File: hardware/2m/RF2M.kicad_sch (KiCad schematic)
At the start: 0 parts

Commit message: Preserve M5A-R1 VHF electrical candidate and review evidence
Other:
- removed sheet 04 2S boost and regulated MMIC rail continued
- note added: "M5A-R1: 144 MHz TRUE AM / EVALUATION SCHEMATIC / NOT RELEASED 1 W ERP sizing: 1.259 W connector carrier, 4.079 W PEP at m=0.80. 2S BOOST or 4S BUCK exclusive populations; training needs only controller 3.3 V. BLOCKING: ST VHF matching not traced; PD54008 PowerFLAT numeric pads OPEN. NO LAYOUT. OPEN: hot SOA, analog loop, RF AM and physical driver-fault response. No PCB/layout/Gerbers/procurement.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"
- note removed: "M5A-R0: 144 MHz TRUE AM / EVALUATION SCHEMATIC / NOT RELEASED\n1 W ERP sizing: 1.259 W connector carrier, 4.079 W PEP at m=0.80.\n2S BOOST or 4S BUCK exclusive populations; training needs only controller 3.3 V.\nOPEN: large-signal matching, hot SOA, critical package geometry, analog loop stability.\nNo PCB/layout/Gerbers/procurement. All physical results NOT_RUN. See docs/M5_2M_REVIEW_DECISION.md."

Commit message: Preserve M5A-R3 historical transmitter schematic and review
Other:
- removed sheet 04 2S boost and regulated MMIC rail
- removed sheet 05 Sine reconstruction and series AM modulator
- removed sheet 05 Sine reconstruction and series AM modulator continued
- removed sheet 06 144MHz source, driver, final matching and output filter
- removed sheet 06 144MHz source, driver, final matching and output filter continued
- removed sheet 09 External supply declarations and measurement contract
- added sheet 04 2S boost,10.9/13.8V candidate (04_boost.kicad_sch)
- added sheet 05 Sine reconstruction and training command (05_pwm_training_command.kicad_sch)
- added sheet 06 DL3BBX retained72MHz doubler, driver, final and output network (06_dl3_rf.kicad_sch)
- added sheet 06b Retained DL3BBX T3 doubler and T4 driver (06b_dl3_doubler_driver.kicad_sch)
- added sheet 06c Retained DL3BBX MRF237 final and output matching/filter (06c_dl3_final.kicad_sch)
- added sheet 10 Original Darlington collector-supply AM, PWM sine input (10_original_modulator.kicad_sch)
- added sheet 11 External supply declarations and qualification boundary (11_external_contract.kicad_sch)
- note added: "M5A-R3 PRIVATE DL3BBX REFERENCE DERIVATIVE / NOT RELEASED Original72-to144MHz doubler,2N4427 driver,MRF237 final and matching retained. Si5351 CLK0=RF/2; CLK2=RF. No premium MMIC and no speculative LDMOS matching. BLOCKING: exact RF transistor procurement/manufacturer and some package/magnetic geometry. Published >3WPEP is not proof of requested5.135WPEP connector capability. All RF/AM/thermal/en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"
- note removed: "M5A-R1: 144 MHz TRUE AM / EVALUATION SCHEMATIC / NOT RELEASED 1 W ERP sizing: 1.259 W connector carrier, 4.079 W PEP at m=0.80. 2S BOOST or 4S BUCK exclusive populations; training needs only controller 3.3 V. BLOCKING: ST VHF matching not traced; PD54008 PowerFLAT numeric pads OPEN. NO LAYOUT. OPEN: hot SOA, analog loop, RF AM and physical driver-fault response. No PCB/layout/Gerbers/procurement.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"

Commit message: Preserve M5A-R4 economical VHF electrical review baseline
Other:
- sheet 11 External supply declarations and qualification boundary renamed 11 External supplies and integrated commissioning
- removed sheet 04 2S boost,10.9/13.8V candidate
- removed sheet 05 Sine reconstruction and training command
- removed sheet 06 DL3BBX retained72MHz doubler, driver, final and output network
- removed sheet 06b Retained DL3BBX T3 doubler and T4 driver
- removed sheet 06c Retained DL3BBX MRF237 final and output matching/filter
- removed sheet 10 Original Darlington collector-supply AM, PWM sine input
- added sheet 04 2S boost and regulated MMIC rail (04_boost_driver_supply.kicad_sch)
- added sheet 05 Sine reconstruction and series AM modulator (05_am.kicad_sch)
- added sheet 05 Sine reconstruction and series AM modulator continued (05_amb1.kicad_sch)
- added sheet 06 Source filter, economical driver and fixed bias (06_source_driver_bias.kicad_sch)
- added sheet 06 Source filter, economical driver and fixed bias continued (06_source_driver_biasb1.kicad_sch)
- added sheet 06b ST final-stage matching derivative (06b_st_matching.kicad_sch)
- added sheet 06c Original ST elliptic harmonic LPF (06c_st_lpf.kicad_sch)
- added sheet 10 Local physical switches and clock sequencing (10_enable_detail.kicad_sch)
- note added: "M5A-R4 / ONE INTEGRATED TRUE-AM CANDIDATE / NOT RELEASED ST PD54008L-E output network and elliptic LPF traced; PHA-1 interstage adaptation unqualified. 2S BOOST9Vfixed OR4S BUCK9Vfull/7.5Vreduced;exclusive populations. Training3.3V only. No obsolete multiplier chain or adjustable RF coils. Full RF/AM/thermal acceptance NOT_RUN. OPEN reservoir/coil/connector definitions and changed interstage matc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"
- note removed: "M5A-R3 PRIVATE DL3BBX REFERENCE DERIVATIVE / NOT RELEASED Original72-to144MHz doubler,2N4427 driver,MRF237 final and matching retained. Si5351 CLK0=RF/2; CLK2=RF. No premium MMIC and no speculative LDMOS matching. BLOCKING: exact RF transistor procurement/manufacturer and some package/magnetic geometry. Published >3WPEP is not proof of requested5.135WPEP connector capability. All RF/AM/thermal/en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"

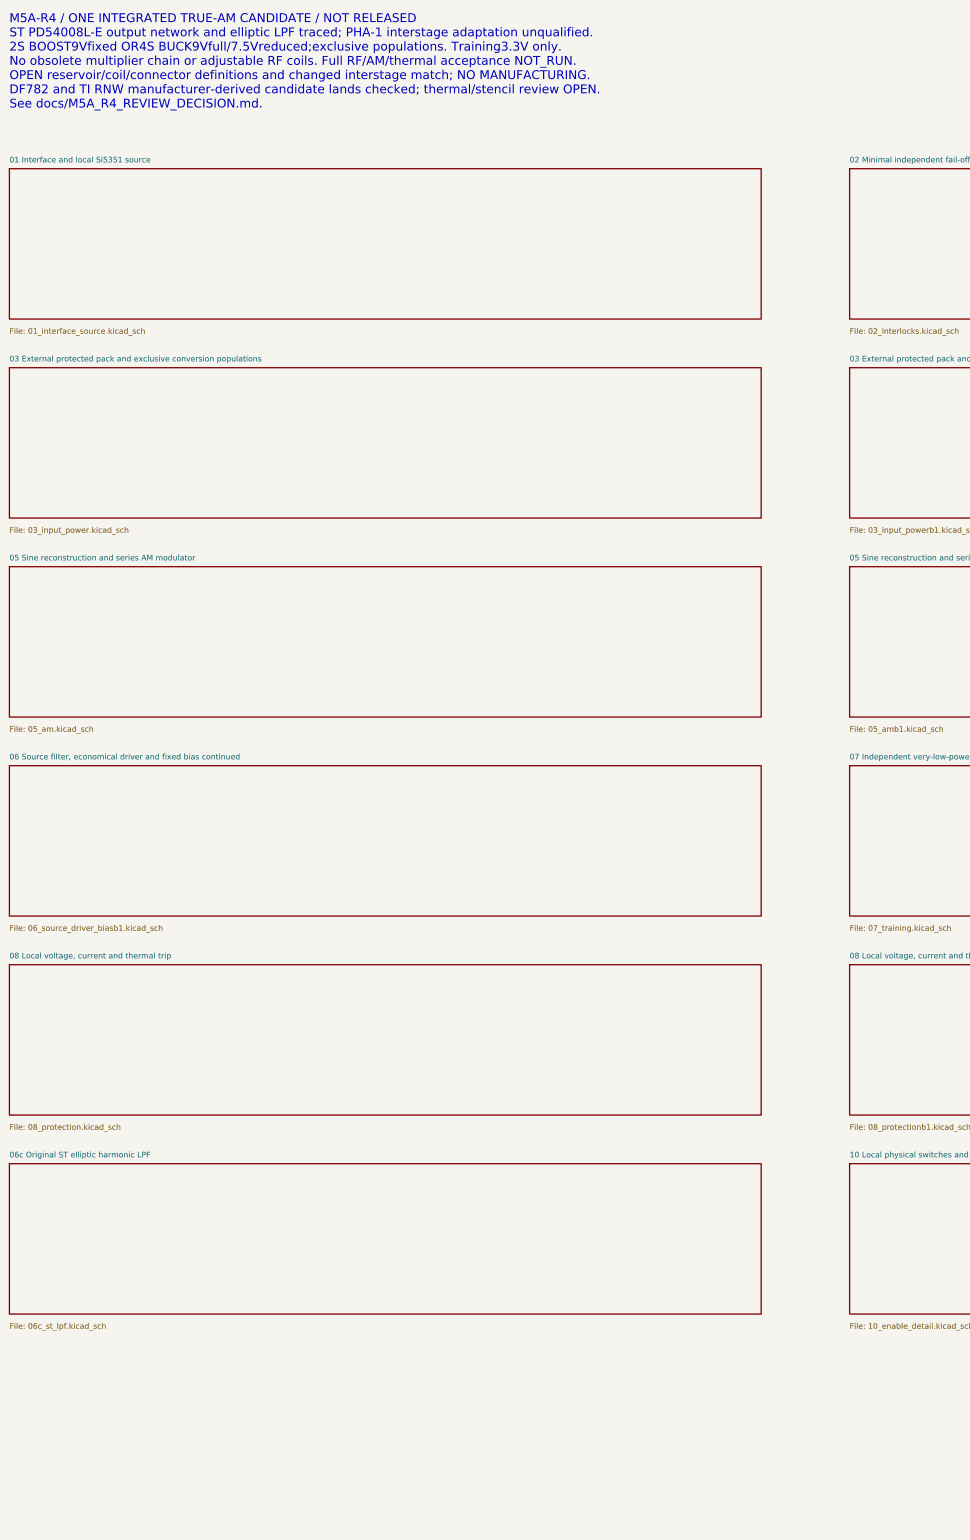
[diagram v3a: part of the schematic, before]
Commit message: Preserve M5B-E1 integrated RF2M evaluation baseline
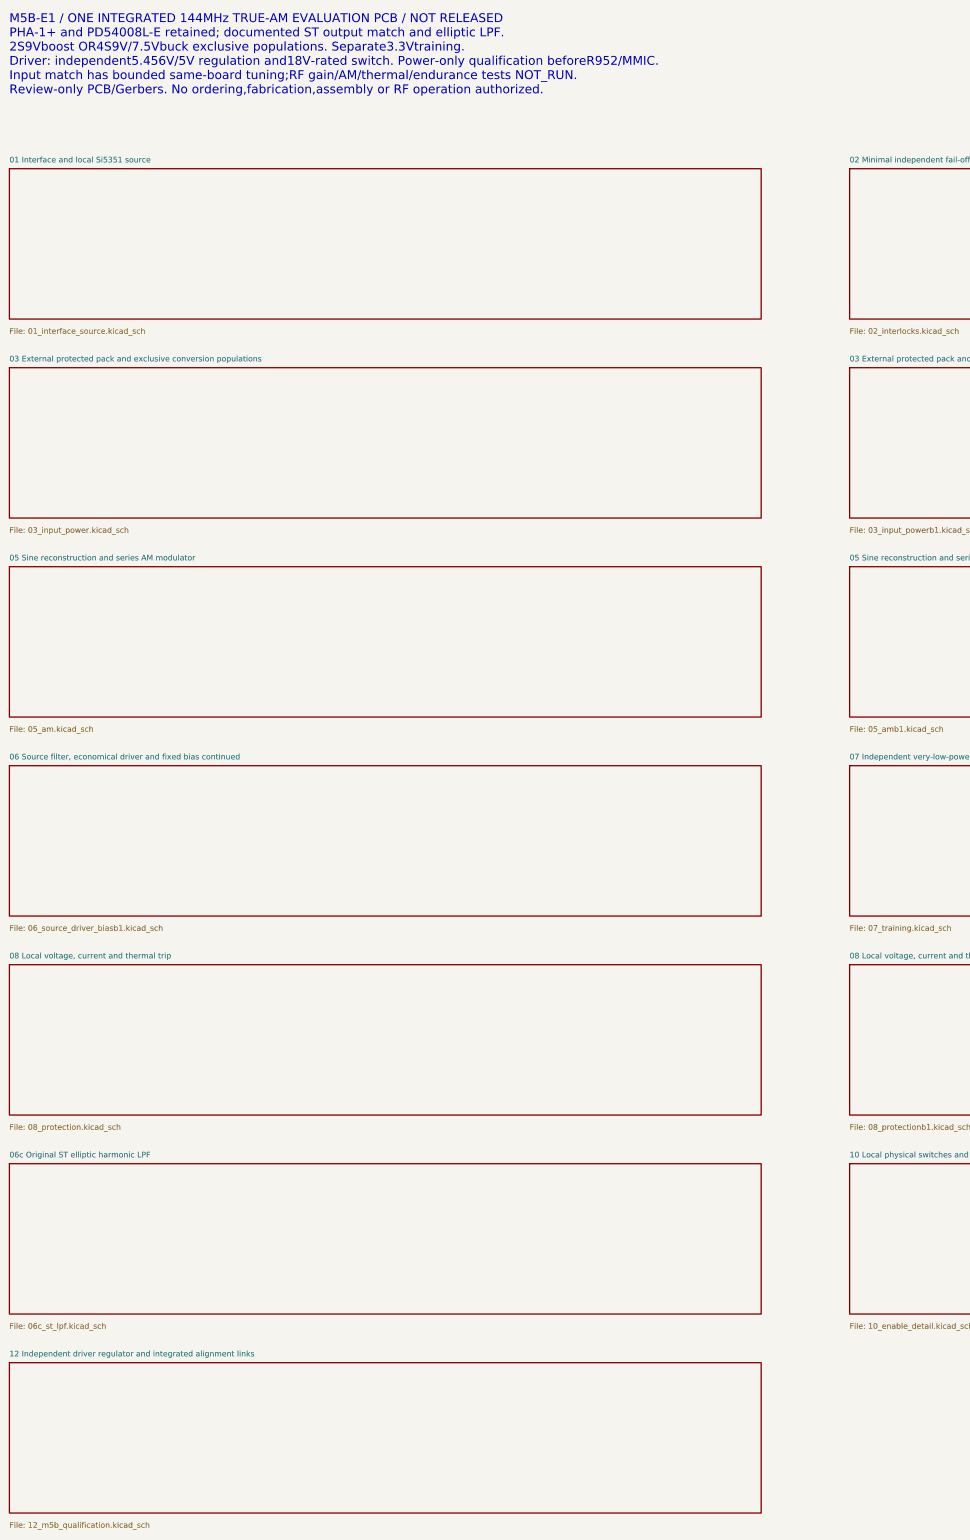
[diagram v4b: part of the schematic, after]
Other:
- added sheet 12 Independent driver regulator and integrated alignment links (12_m5b_qualification.kicad_sch)
- note added: "M5B-E1 / ONE INTEGRATED 144MHz TRUE-AM EVALUATION PCB / NOT RELEASED PHA-1+ and PD54008L-E retained; documented ST output match and elliptic LPF. 2S9Vboost OR4S9V/7.5Vbuck exclusive populations. Separate3.3Vtraining. Driver: independent5.456V/5V regulation and18V-rated switch. Power-only qualification beforeR952/MMIC. Input match has bounded same-board tuning;RF gain/AM/thermal/endurance tests NO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"
- note removed: "M5A-R4 / ONE INTEGRATED TRUE-AM CANDIDATE / NOT RELEASED ST PD54008L-E output network and elliptic LPF traced; PHA-1 interstage adaptation unqualified. 2S BOOST9Vfixed OR4S BUCK9Vfull/7.5Vreduced;exclusive populations. Training3.3V only. No obsolete multiplier chain or adjustable RF coils. Full RF/AM/thermal acceptance NOT_RUN. OPEN reservoir/coil/connector definitions and changed interstage matc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"

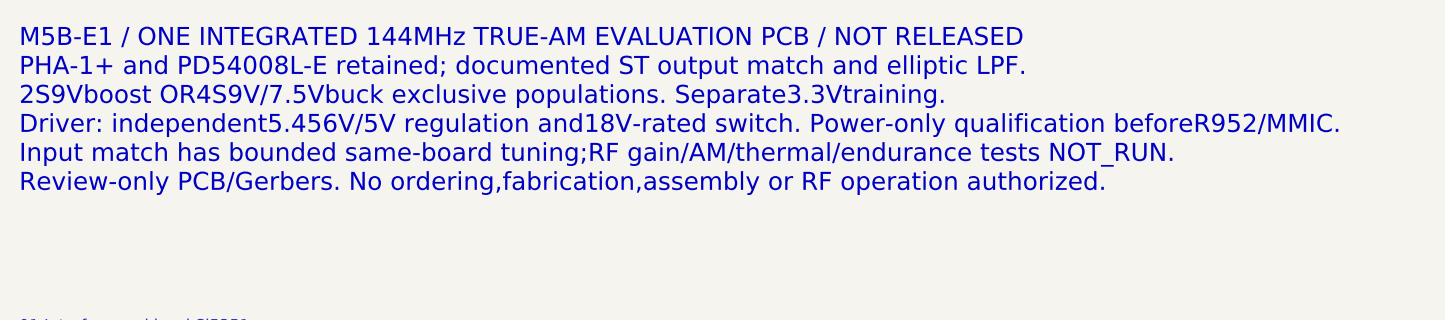
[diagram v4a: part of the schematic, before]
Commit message: Implement M5B-E3 standard JLCPCB RF2M evaluation board
Recalculate and implement 1.6 mm / 1 oz RF geometry, power copper, thermal vias, connector holes and manufacturing legend. Preserve electrical functions and population variants. Add native-geometry DFM, regression checks and fresh native/fabrication review archives. CAD milestone only; no manufacturing or operational release.
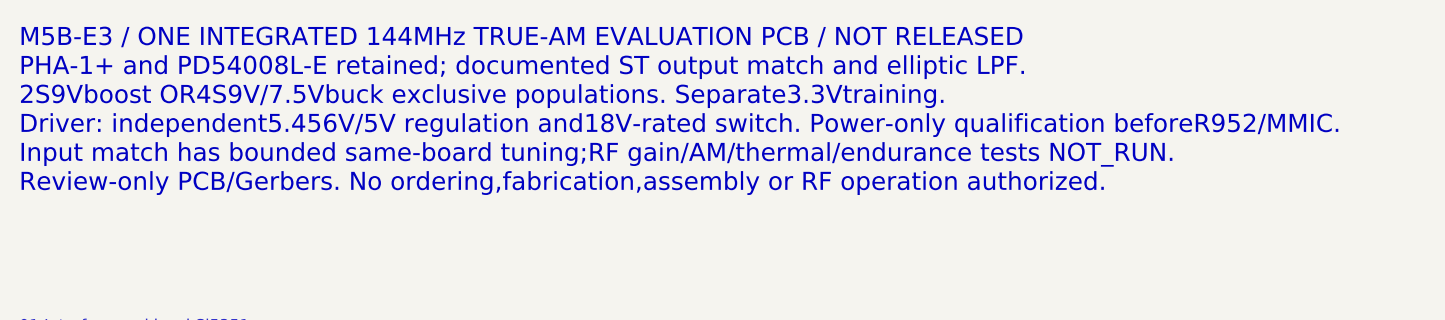
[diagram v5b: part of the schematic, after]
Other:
- note added: "M5B-E3 / ONE INTEGRATED 144MHz TRUE-AM EVALUATION PCB / NOT RELEASED PHA-1+ and PD54008L-E retained; documented ST output match and elliptic LPF. 2S9Vboost OR4S9V/7.5Vbuck exclusive populations. Separate3.3Vtraining. Driver: independent5.456V/5V regulation and18V-rated switch. Power-only qualification beforeR952/MMIC. Input match has bounded same-board tuning;RF gain/AM/thermal/endurance tests NO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"
- note removed: "M5B-E1 / ONE INTEGRATED 144MHz TRUE-AM EVALUATION PCB / NOT RELEASED PHA-1+ and PD54008L-E retained; documented ST output match and elliptic LPF. 2S9Vboost OR4S9V/7.5Vbuck exclusive populations. Separate3.3Vtraining. Driver: independent5.456V/5V regulation and18V-rated switch. Power-only qualification beforeR952/MMIC. Input match has bounded same-board tuning;RF gain/AM/thermal/endurance tests NO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"

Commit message: Implement M5B-E4 thermal candidate with source-joint assembly hold
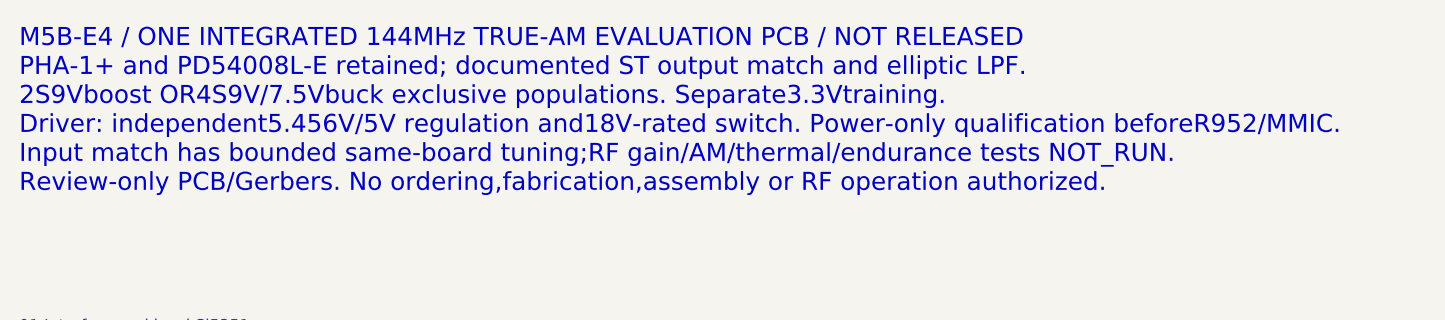
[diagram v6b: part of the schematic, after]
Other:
- note added: "M5B-E4 / ONE INTEGRATED 144MHz TRUE-AM EVALUATION PCB / NOT RELEASED PHA-1+ and PD54008L-E retained; documented ST output match and elliptic LPF. 2S9Vboost OR4S9V/7.5Vbuck exclusive populations. Separate3.3Vtraining. Driver: independent5.456V/5V regulation and18V-rated switch. Power-only qualification beforeR952/MMIC. Input match has bounded same-board tuning;RF gain/AM/thermal/endurance tests NO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"
- note removed: "M5B-E3 / ONE INTEGRATED 144MHz TRUE-AM EVALUATION PCB / NOT RELEASED PHA-1+ and PD54008L-E retained; documented ST output match and elliptic LPF. 2S9Vboost OR4S9V/7.5Vbuck exclusive populations. Separate3.3Vtraining. Driver: independent5.456V/5V regulation and18V-rated switch. Power-only qualification beforeR952/MMIC. Input match has bounded same-board tuning;RF gain/AM/thermal/endurance tests NO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"

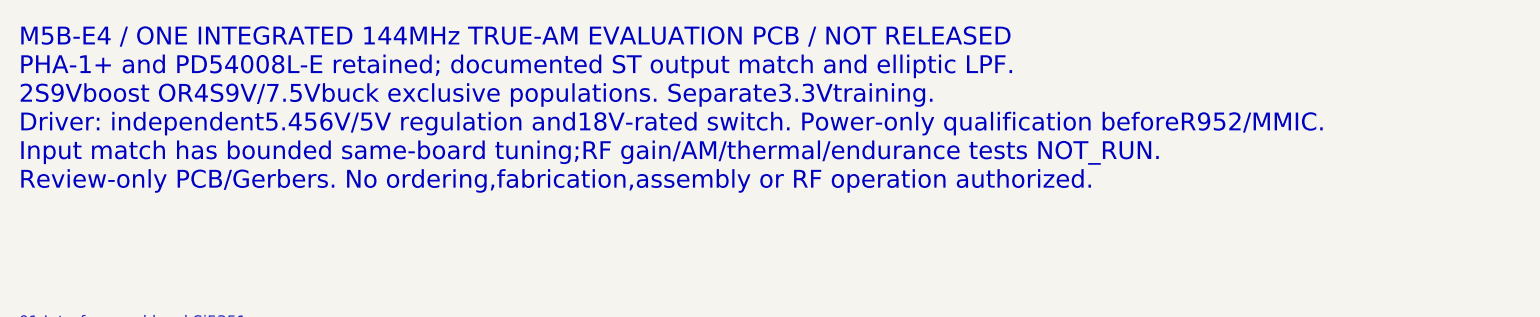
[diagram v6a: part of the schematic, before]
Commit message: Implement M5B-E4R1 source-joint prototype candidate
Replace source mask islands with a controlled open-via hybrid and native-derived local stencil. Preserve standard JLCPCB and RF circuitry. Add assembly qualification, thermal convergence and adverse sensitivities, native DFM/mutation checks and fresh review exports. Conservative 110 C target is missed; 125 C physical gate stays open. No acceptance tag or manufacturing authorization.
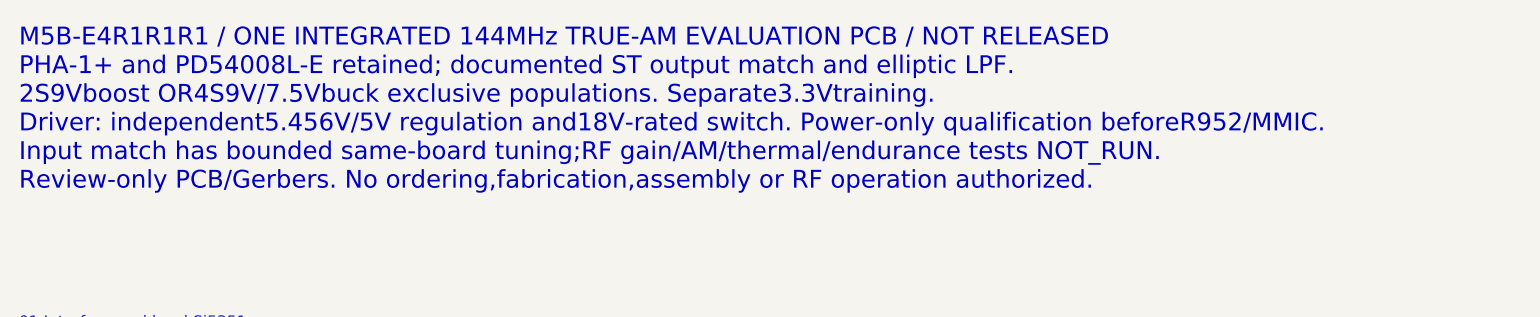
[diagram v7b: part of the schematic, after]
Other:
- note added: "M5B-E4R1R1R1 / ONE INTEGRATED 144MHz TRUE-AM EVALUATION PCB / NOT RELEASED PHA-1+ and PD54008L-E retained; documented ST output match and elliptic LPF. 2S9Vboost OR4S9V/7.5Vbuck exclusive populations. Separate3.3Vtraining. Driver: independent5.456V/5V regulation and18V-rated switch. Power-only qualification beforeR952/MMIC. Input match has bounded same-board tuning;RF gain/AM/thermal/endurance te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"
- note removed: "M5B-E4 / ONE INTEGRATED 144MHz TRUE-AM EVALUATION PCB / NOT RELEASED PHA-1+ and PD54008L-E retained; documented ST output match and elliptic LPF. 2S9Vboost OR4S9V/7.5Vbuck exclusive populations. Separate3.3Vtraining. Driver: independent5.456V/5V regulation and18V-rated switch. Power-only qualification beforeR952/MMIC. Input match has bounded same-board tuning;RF gain/AM/thermal/endurance tests NO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"

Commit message: M5B-E5: compact RF2M to the shared 150x110 mm platform
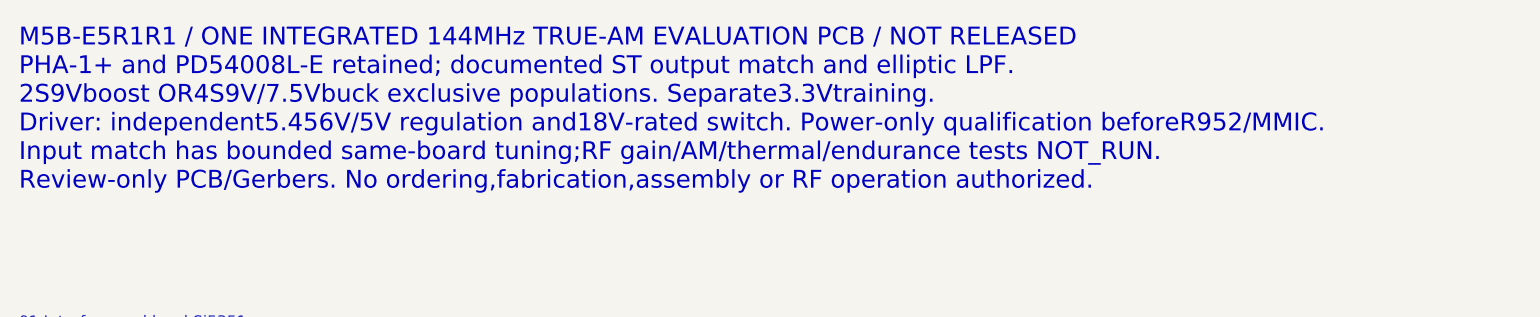
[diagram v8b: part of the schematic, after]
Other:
- note added: "M5B-E5R1R1 / ONE INTEGRATED 144MHz TRUE-AM EVALUATION PCB / NOT RELEASED PHA-1+ and PD54008L-E retained; documented ST output match and elliptic LPF. 2S9Vboost OR4S9V/7.5Vbuck exclusive populations. Separate3.3Vtraining. Driver: independent5.456V/5V regulation and18V-rated switch. Power-only qualification beforeR952/MMIC. Input match has bounded same-board tuning;RF gain/AM/thermal/endurance test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"
- note removed: "M5B-E4R1R1R1 / ONE INTEGRATED 144MHz TRUE-AM EVALUATION PCB / NOT RELEASED PHA-1+ and PD54008L-E retained; documented ST output match and elliptic LPF. 2S9Vboost OR4S9V/7.5Vbuck exclusive populations. Separate3.3Vtraining. Driver: independent5.456V/5V regulation and18V-rated switch. Power-only qualification beforeR952/MMIC. Input match has bounded same-board tuning;RF gain/AM/thermal/endurance te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"
